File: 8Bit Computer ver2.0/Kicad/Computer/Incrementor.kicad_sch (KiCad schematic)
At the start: 12 parts, among them IC134 SN74ABT245BDWR, IC135 SN74LVC1G32DBVR, IC136 SN74LVC1G14DBVR, IC137 SN74LVC1G14DBVR, IC138 SN74AHC74DR, IC139 SN74F283D, IC140 SN74F283D, IC141 SN74F283D, IC142 SN74LVC1G86DBVR, IC143 SN74ABT574ADWR, IC144 SN74ABT574ADWR, IC145 SN74LVC1G14DBVR

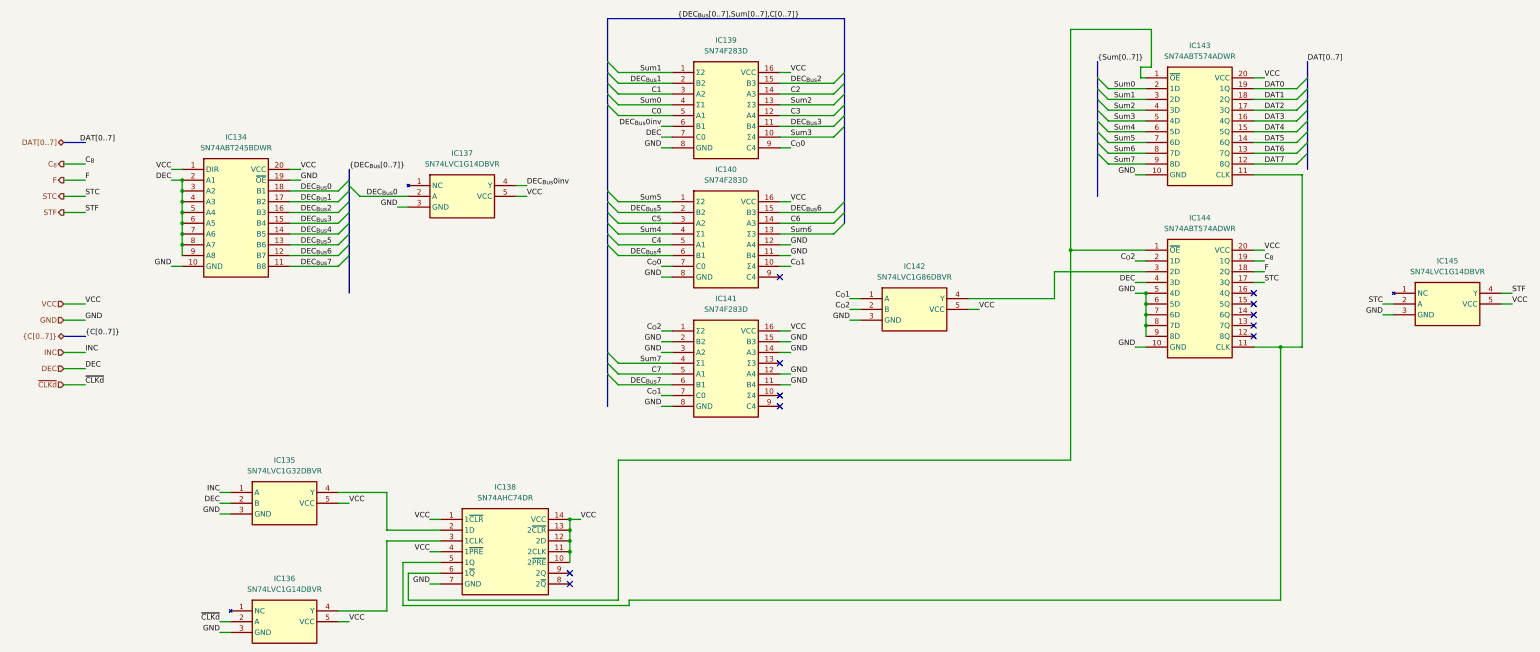
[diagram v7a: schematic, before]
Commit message: Kicad, parts
parts:
added Mux 4:1 for CLK
added LM555
Kicad:
added some Diodes for Flash disable
fixed wrong routing of flag register
fixed wrong routing of STC STF in INC/AddS
LM555 circuit for 1Hz to 100Hz
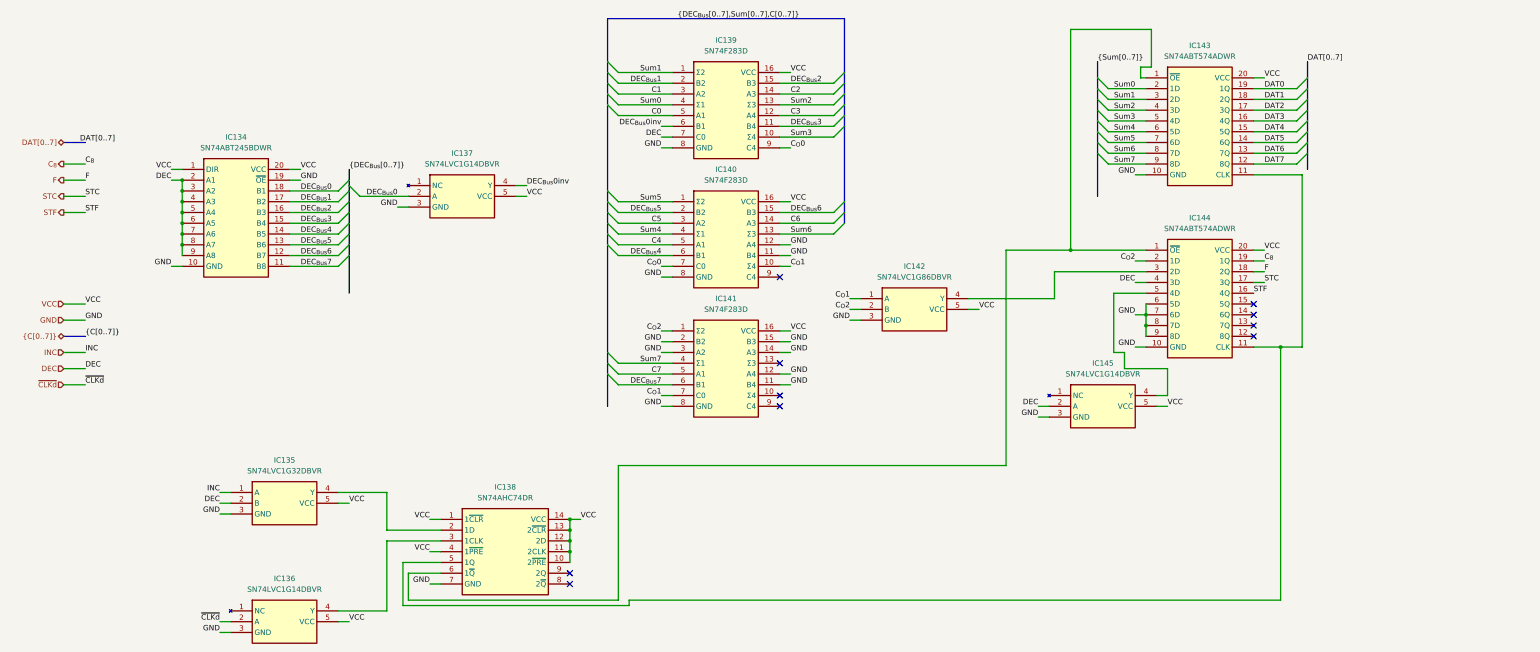
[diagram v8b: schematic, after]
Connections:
- net DEC: now also IC145.2 (A)
- net GND: no longer IC144.5 (4D)
- net STC: no longer IC145.2 (A)
- net STF: now also IC144.16 (4Q); no longer IC145.4 (Y)
- new net: IC144.5 (4D), IC145.4 (Y)
- no-connect marks 11 -> 10
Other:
- moved on the sheet: IC145
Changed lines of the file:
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@@
 	)
 	(junction
-		(at 278.13 96.52)
-		(diameter 0)
-		(color 0 0 0 0)
-	)
-	(junction
 		(at 50.8 72.39)
 		(diameter 0)
@@
 		(color 0 0 0 0)
 	)
-	(junction
-		(at 278.13 99.06)
-		(diameter 0)
-		(color 0 0 0 0)
-	)
-	(no_connect
-		(at 303.53 96.52)
-	)
 	(no_connect
 		(at 191.77 120.65)
@@
 	(wire
 		(pts
+			(xy 273.05 114.3) (xy 273.05 110.49)
+		)
+		(stroke
+			(width 0)
+			(type default)
+		)
+	)
+	(wire
+		(pts
 			(xy 142.24 157.48) (xy 142.24 160.02)
 		)
@@
 	(wire
 		(pts
+			(xy 283.21 120.65) (xy 283.21 114.3)
+		)
+		(stroke
+			(width 0)
+			(type default)
+		)
+	)
+	(wire
+		(pts
 			(xy 50.8 82.55) (xy 50.8 85.09)
 		)
@@
 	(wire
 		(pts
+			(xy 273.05 110.49) (xy 270.51 110.49)
+		)
+		(stroke
+			(width 0)
+			(type default)
+		)
+	)
+	(wire
+		(pts
 			(xy 153.67 85.09) (xy 166.37 85.09)
 		)
@@
 	(wire
 		(pts
-			(xy 361.95 99.06) (xy 364.49 99.06)
+			(xy 280.67 123.19) (xy 283.21 123.19)
 		)
 		(stroke
@@
 	(wire
 		(pts
+			(xy 275.59 101.6) (xy 278.13 101.6)
+		)
+		(stroke
+			(width 0)
+			(type default)
+		)
+	)
+	(wire
+		(pts
 			(xy 309.88 109.22) (xy 303.53 109.22)
 		)
@@
 	(wire
 		(pts
-			(xy 204.47 46.99) (xy 191.77 46.99)
-		)
-		(stroke
-			(width 0)
-			(type default)
-		)
-	)
-	(bus
-		(pts
-			(xy 316.23 60.96) (xy 316.23 63.5)
+			(xy 270.51 96.52) (xy 278.13 96.52)
 		)
 		(stroke
@@
 	(wire
 		(pts
-			(xy 276.86 43.18) (xy 276.86 45.72)
+			(xy 204.47 46.99) (xy 191.77 46.99)
 		)
 		(stroke
@@
 		)
 	)
-	(wire
+	(bus
 		(pts
-			(xy 50.8 80.01) (xy 50.8 82.55)
+			(xy 316.23 60.96) (xy 316.23 63.5)
 		)
 		(stroke
@@
 	(wire
 		(pts
-			(xy 59.69 148.59) (xy 62.23 148.59)
+			(xy 276.86 43.18) (xy 276.86 45.72)
 		)
 		(stroke
@@
 	(wire
 		(pts
-			(xy 204.47 82.55) (xy 191.77 82.55)
+			(xy 50.8 80.01) (xy 50.8 82.55)
 		)
 		(stroke
@@
 	(wire
 		(pts
-			(xy 278.13 96.52) (xy 278.13 99.06)
+			(xy 59.69 148.59) (xy 62.23 148.59)
 		)
 		(stroke
@@
 	(wire
 		(pts
-			(xy 275.59 96.52) (xy 278.13 96.52)
+			(xy 204.47 82.55) (xy 191.77 82.55)
 		)
 		(stroke
@@
 	(wire
 		(pts
-			(xy 153.67 168.91) (xy 153.67 135.89)
+			(xy 153.67 168.91) (xy 153.67 137.16)
 		)
 		(stroke
@@
 	(wire
 		(pts
-			(xy 336.55 99.06) (xy 334.01 99.06)
+			(xy 255.27 123.19) (xy 252.73 123.19)
 		)
 		(stroke
@@
 	(wire
 		(pts
+			(xy 270.51 110.49) (xy 270.51 96.52)
+		)
+		(stroke
+			(width 0)
+			(type default)
+		)
+	)
+	(wire
+		(pts
 			(xy 204.47 77.47) (xy 191.77 77.47)
 		)
@@
 	(wire
 		(pts
-			(xy 260.35 135.89) (xy 260.35 86.36)
+			(xy 245.11 86.36) (xy 245.11 137.16)
 		)
 		(stroke
@@
 	(wire
 		(pts
-			(xy 361.95 96.52) (xy 364.49 96.52)
+			(xy 280.67 120.65) (xy 283.21 120.65)
 		)
 		(stroke
@@
 	(wire
 		(pts
-			(xy 334.01 101.6) (xy 336.55 101.6)
+			(xy 252.73 125.73) (xy 255.27 125.73)
 		)
 		(stroke
@@
 		)
 	)
+	(wire
+		(pts
+			(xy 245.11 86.36) (xy 260.35 86.36)
+		)
+		(stroke
+			(width 0)
+			(type default)
+		)
+	)
 	(bus
 		(pts
@@
 		)
 	)
+	(wire
+		(pts
+			(xy 283.21 114.3) (xy 273.05 114.3)
+		)
+		(stroke
+			(width 0)
+			(type default)
+		)
+	)
 	(bus
 		(pts
@@
 	(wire
 		(pts
-			(xy 153.67 135.89) (xy 260.35 135.89)
+			(xy 153.67 137.16) (xy 245.11 137.16)
 		)
 		(stroke
@@
 	)
 	(label "VCC"
-		(at 364.49 99.06 0)
+		(at 283.21 123.19 0)
 		(effects
 			(font
@@
 		)
 	)
-	(label "STF"
-		(at 364.49 96.52 0)
-		(effects
-			(font
-				(size 1.27 1.27)
-			)
-			(justify left bottom)
-		)
-	)
 	(label "DEC"
 		(at 48.26 69.85 180)
@@
 		)
 	)
+	(label "DEC"
+		(at 252.73 123.19 180)
+		(effects
+			(font
+				(size 1.27 1.27)
+			)
+			(justify right bottom)
+		)
+	)
 	(label "GND"
 		(at 275.59 68.58 180)
@@
 		)
 	)
+	(label "GND"
+		(at 275.59 101.6 180)
+		(effects
+			(font
+				(size 1.27 1.27)
+			)
+			(justify right bottom)
+		)
+	)
 	(label "Sum3"
 		(at 275.59 55.88 180)
@@
 		)
 	)
-	(label "STC"
-		(at 334.01 99.06 180)
-		(effects
-			(font
-				(size 1.27 1.27)
-			)
-			(justify right bottom)
-		)
-	)
 	(label "DEC_{Bus}0"
 		(at 101.6 73.66 180)
@@
 	)
 	(label "GND"
-		(at 334.01 101.6 180)
+		(at 252.73 125.73 180)
 		(effects
 			(font
@@
 	)
 	(label "GND"
-		(at 275.59 96.52 180)
-		(effects
-			(font
-				(size 1.27 1.27)
-			)
-			(justify right bottom)
-		)
-	)
-	(label "GND"
 		(at 59.69 148.59 180)
 		(effects
@@
 		)
 	)
+	(label "STF"
+		(at 303.53 96.52 0)
+		(effects
+			(font
+				(size 1.27 1.27)
+			)
+			(justify left bottom)
+		)
+	)
 	(label "Sum0"
 		(at 163.83 52.07 180)
@@
 	(symbol
 		(lib_id "Samacsys:SN74LVC1G14DBVR")
-		(at 336.55 96.52 0)
+		(at 255.27 120.65 0)
 		(unit 1)
 		(exclude_from_sim no)
@@
 		(fields_autoplaced yes)
 		(property "Reference" "IC145"
-			(at 349.25 88.9 0)
+			(at 267.97 113.03 0)
 			(effects
 				(font
@@
 		)
 		(property "Value" "SN74LVC1G14DBVR"
-			(at 349.25 91.44 0)
+			(at 267.97 115.57 0)
 			(effects
 				(font
@@
 		)
 		(property "Footprint" "Samacsys:SOT95P280X145-5N"
-			(at 358.14 191.44 0)
+			(at 276.86 215.57 0)
 			(effects
 				(font
@@
 		)
 		(property "Datasheet" "https://datasheet.datasheetarchive.com/originals/distributors/Datasheets-DGA13/1136296.pdf"
-			(at 358.14 291.44 0)
+			(at 276.86 315.57 0)
 			(effects
 				(font
@@
 		)
 		(property "Description" "TEXAS INSTRUMENTS - SN74LVC1G14DBVR - IC, SCHMITT TRIGGER INVERTER, SMD"
-			(at 336.55 96.52 0)
+			(at 255.27 120.65 0)
 			(effects
 				(font
@@
 		)
 		(property "Height" "1.45"
-			(at 358.14 491.44 0)
+			(at 276.86 515.57 0)
 			(effects
 				(font
@@
 		)
 		(property "Mouser Part Number" "595-SN74LVC1G14DBVR"
-			(at 358.14 591.44 0)
+			(at 276.86 615.57 0)
 			(effects
 				(font
@@
 		)
 		(property "Mouser Price/Stock" "https://www.mouser.co.uk/ProductDetail/Texas-Instruments/SN74LVC1G14DBVR?qs=dT9u2OTAaVWRIgCrQFnxuQ%3D%3D"
-			(at 358.14 691.44 0)
+			(at 276.86 715.57 0)
 			(effects
 				(font
@@
 		)
 		(property "Manufacturer_Name" "Texas Instruments"
-			(at 358.14 791.44 0)
+			(at 276.86 815.57 0)
 			(effects
 				(font
@@
 		)
 		(property "Manufacturer_Part_Number" "SN74LVC1G14DBVR"
-			(at 358.14 891.44 0)
+			(at 276.86 915.57 0)
 			(effects
 				(font
